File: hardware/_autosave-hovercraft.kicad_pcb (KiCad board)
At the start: 2 copper layers, 50 x 65 mm, 44 parts, among them J1 USB_OTG, J10 CONN_01X02, J11 CONN_01X02, J12 CONN_01X02, J2 CONN_01X03, J3 CONN_01X03, J4 CONN_01X03, J5 CONN_01X03, J6 CONN_01X03, J7 CONN_01X03, J8 CONN_01X02, J9 CONN_01X02, SW1 RESET, SW2 BOOT, U1 HC-12, U2 ATMEGA32U2-AU, Y1 Crystal_GND24

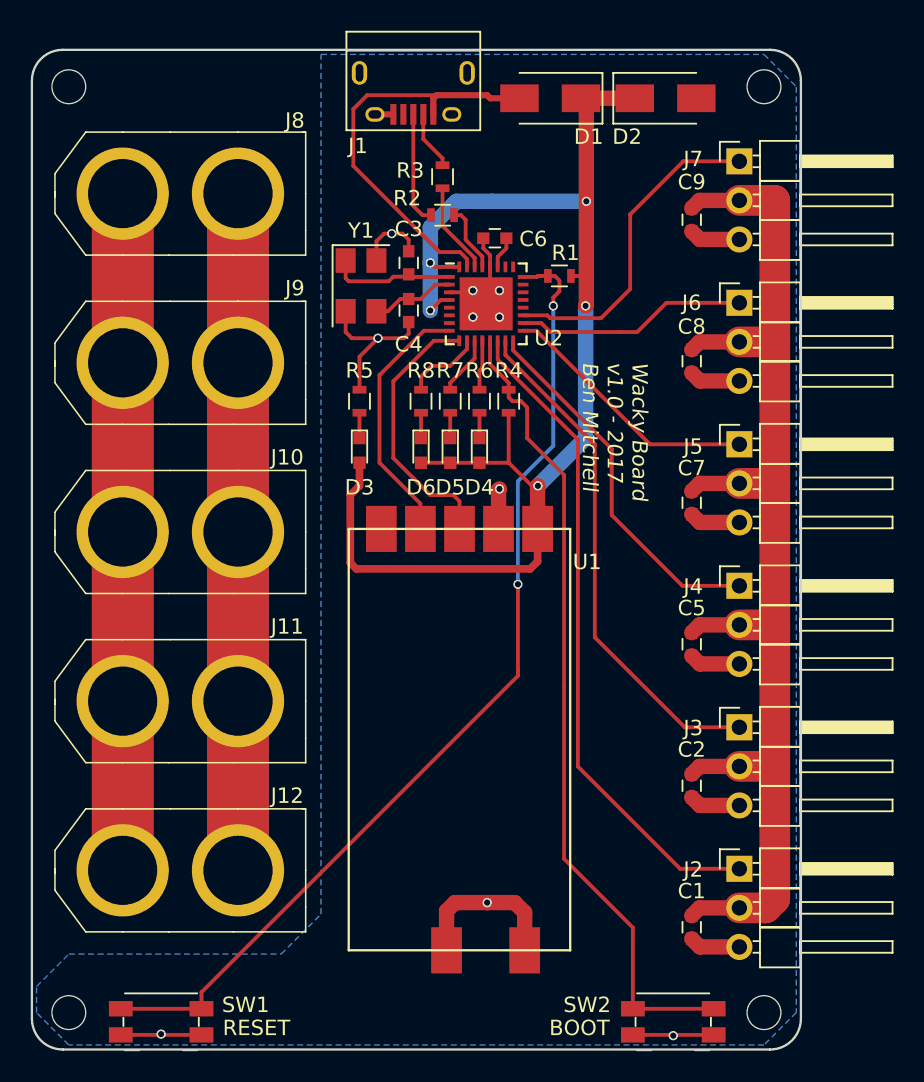
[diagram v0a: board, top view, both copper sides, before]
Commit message: Moved the servo PWM signals to different pins to free up the SPI for a gyroscope/accelerometer/magnetometer
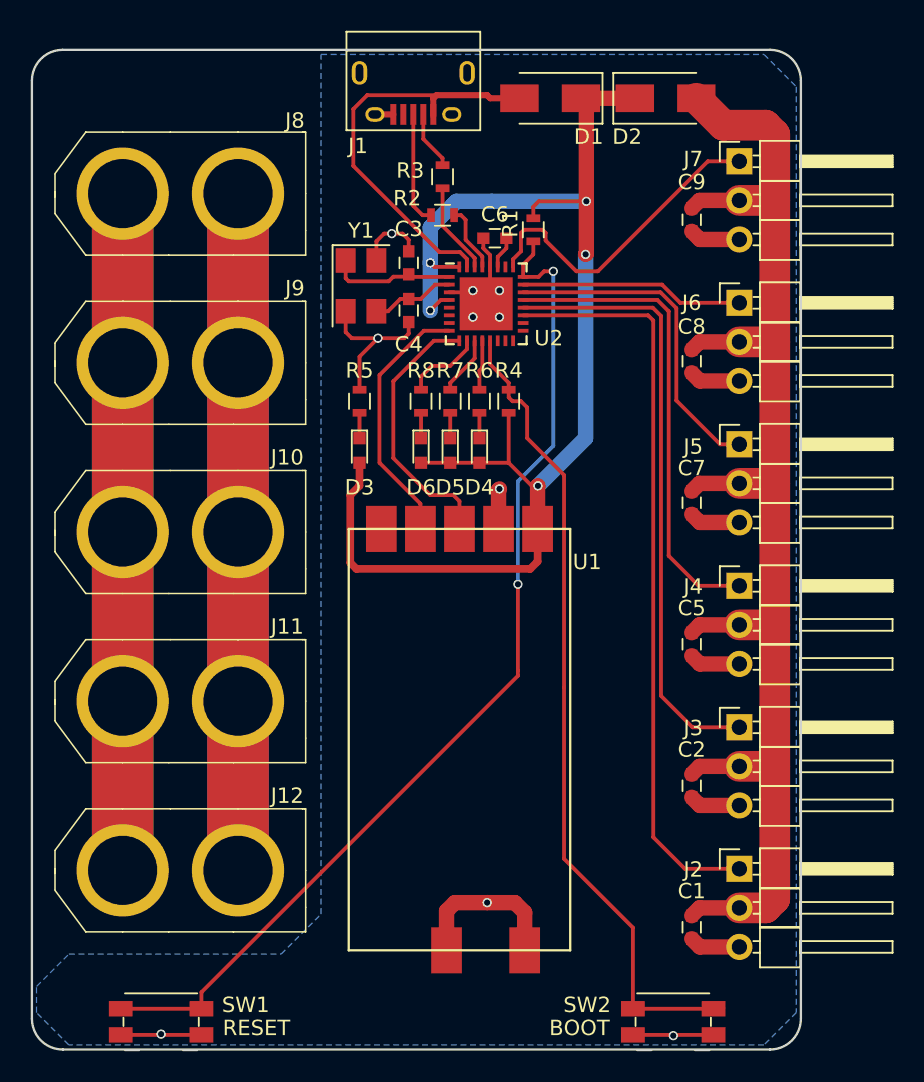
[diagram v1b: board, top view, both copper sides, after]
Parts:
- removed REF** (x4): MountingHole_2.2mm_M2, Mounting_Holes:MountingHole_2.2mm_M2
- moved R1 3.45 mm to (132.7, 111.8), turned to 270 degrees
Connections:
- U2 pad 14: /CH0 -> Net-(U2-Pad14)
- U2 pad 15: /CH1 -> Net-(U2-Pad15)
- U2 pad 16: /CH2 -> Net-(U2-Pad16)
- U2 pad 17: /CH3 -> Net-(U2-Pad17)
- U2 pad 18: /CH4 -> Net-(U2-Pad18)
- U2 pad 19: /CH5 -> /CH0
- U2 pad 20: Net-(U2-Pad20) -> /CH1
- U2 pad 21: Net-(U2-Pad21) -> /CH2
- U2 pad 22: Net-(U2-Pad22) -> /CH3
- U2 pad 23: Net-(U2-Pad23) -> /CH4
- U2 pad 25: Net-(U2-Pad25) -> /CH5
- U2 pad 33: GND -> (no net)
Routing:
- net Net-(C1-Pad1): track 79.3 -> 89.7 mm
- net /CH2: track 24.2 -> 31.1 mm
- net /CH1: track 33.5 -> 39.8 mm
- net /CH0: track 43.1 -> 48.7 mm
- net /CH3: track 17.1 -> 21.7 mm
- net VCC: track 86.6 -> 90.0 mm
- net Net-(R1-Pad2): track 64.8 -> 67.4 mm
- net /CH4: track 15.1 -> 14.6 mm
- net (no net): track 0.00 -> 0.04 mm, vias 0 -> 2
- net GND: vias 10 -> 8
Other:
- board text removed: "Wacky Board v1.0 - 2017 Ben Mitchell"
